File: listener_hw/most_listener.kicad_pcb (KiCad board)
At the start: 2 copper layers, 125 x 80 mm, 153 parts, among them J1 1-1394640-1, J2 ANALYSER, J3 I2S, J4 VBAT_IN, J5 PLR135/T10, J6 PLT133/T10W, J7 RCA 75R, J8 LINE L, J9 LINE R, M1 Tang Nano 20K, M2 ESP32-DevKitC-VIE, U1 74LVC1G34, U10 TPS2553DBVR, U11 74LVC1G123, U12 DIR9001, U13 SRC4192, U14 LP5907MFX-3.3, U15 PCM5102A, U16 LP5907MFX-3.3, U2 74LVC1G157, U3 74LVC1G125, U4 74LVC1G123, U5 TPS7B8133DRV, U6 LMR38020F, U7 Si514, U8 LP5907MFX-3.3, U9 74LVC1G79, X1 24.576MHz

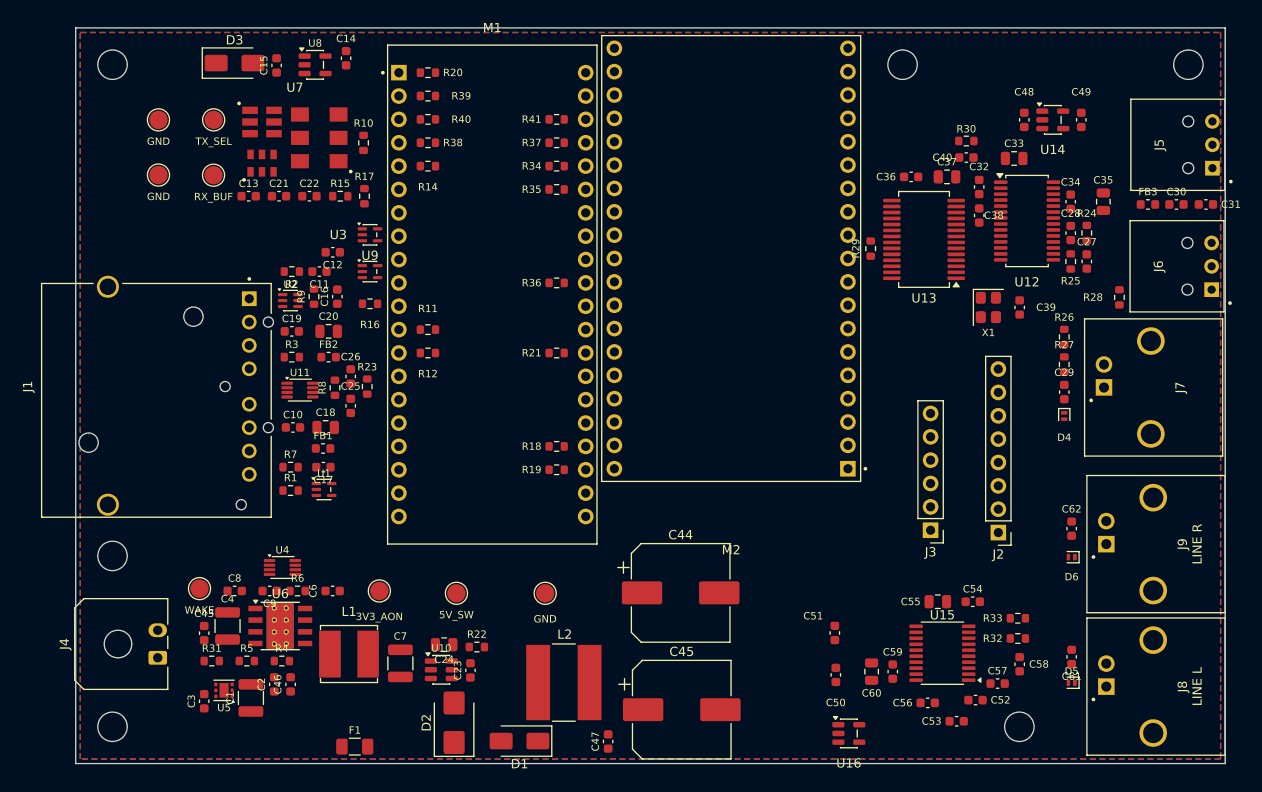
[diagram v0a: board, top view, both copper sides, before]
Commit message: Board: silk pass on the final placement - DRC with no error and no warning
The user settled the placement (moving C44, H4 and M2 a little last) and
asked for the silkscreen to be put right: 94 silk warnings before, none now.

- The edge connectors' own silk no longer reaches the board edge: the MOST
  header (J1), the TOSLINK modules (J5, J6) and the RCA jacks (J7, J8, J9)
  have their outline open on the port side, the sides ending 0.4 mm behind
  the port face (for J1, 0.4 mm inside the edge its foot line marks); the
  board's copies were refreshed from the library, so they match it. J4, a
  KiCad library part, moved 0.6 mm in from the left edge instead.
- Every silk text was placed again: the first spot around its part that
  touches no pad, no silk line and no other text and stays 0.4 mm inside the
  edge - 0.8 mm text for passives, 1.0 mm for ICs, modules and connectors,
  nothing smaller; M1, M2 and J1 carry their names inside their outlines,
  J8/J9 their LINE L/R, the test points their net names. The last three
  (C10, C18, R5) were set by hand.
- H4 back to 4.0 mm from the bottom edge; the antenna keep-out follows M2.

DRC with --schematic-parity: no error, no warning, no difference from the
sheet; 367 unconnected items - the routing is next.

Co-Authored-By: Claude Opus 5.5 <noreply@anthropic.com>
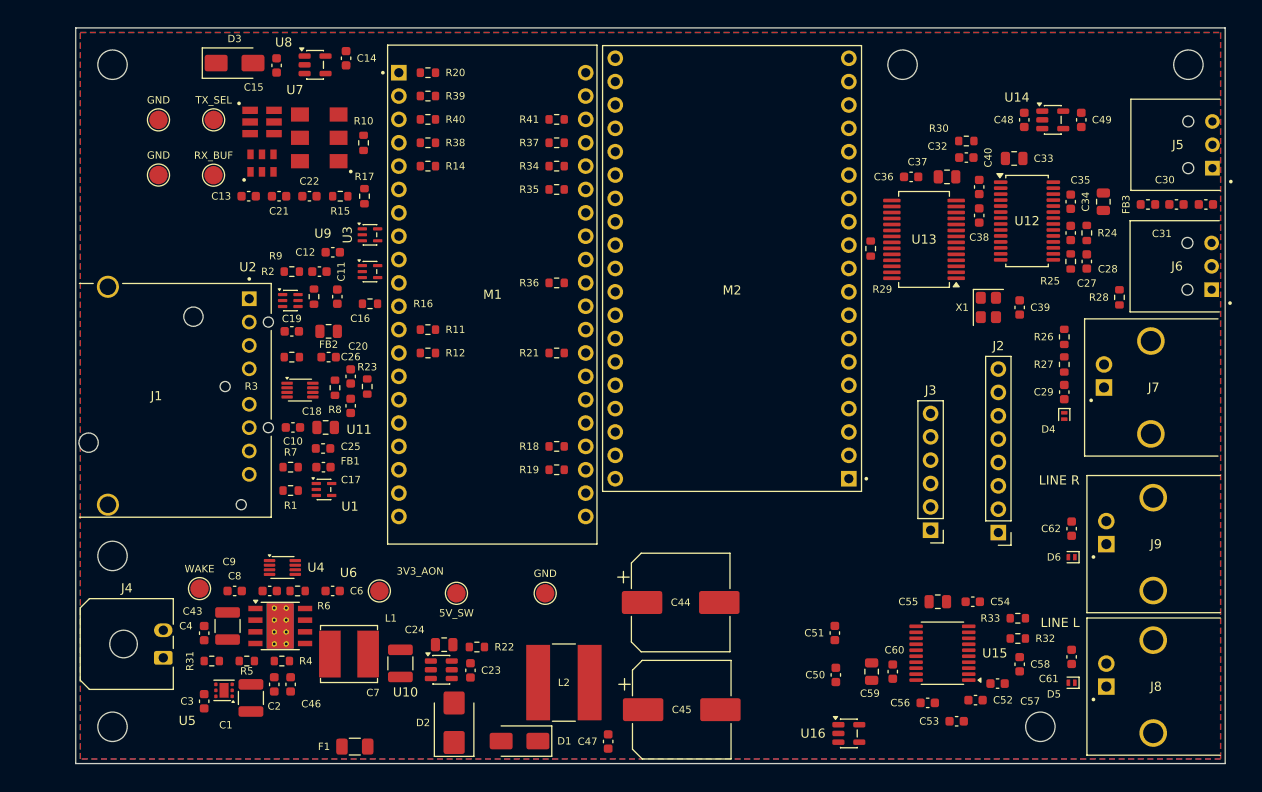
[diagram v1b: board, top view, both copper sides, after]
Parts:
- moved H4 2.29 mm to (104.9, 76.0)
- moved M2 1.09 mm to (71.4, 26.2)
- moved C44 1.04 mm to (65.8, 62.5)
- moved J4 0.60 mm to (9.52, 68.5)

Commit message: Board: routed - one ground plane below, crossed only by short jumpers; signals and supplies on top
- supplies laid by hand: the 5 V trunk 1 mm wide from C7 up the left edge under J1 and along
  the top edge; VBAT from the input caps round the bottom into C43, C4 and U6; 3V3_AON from the
  LDO with two jumpers (1.9 mm under VBAT at C3, 2.4 mm under the trunk into the front end);
  R4's sense on top under L1
- the host switch U10 with C23, C24 and R22 moved to M2's 5 V pin: /5V_HOST no longer crosses
  the signals from M1 to the right half
- a via beside every SMD ground pad; the top pour stitched to the plane about every 6 mm
- signals on top, the crossings as jumpers: 75, 174 mm in all, the longest 6.5 mm; 459 vias
- DRC: no error, no warning, nothing unconnected; the board matches the sheet

Co-Authored-By: Claude Opus 5.5 <noreply@anthropic.com>
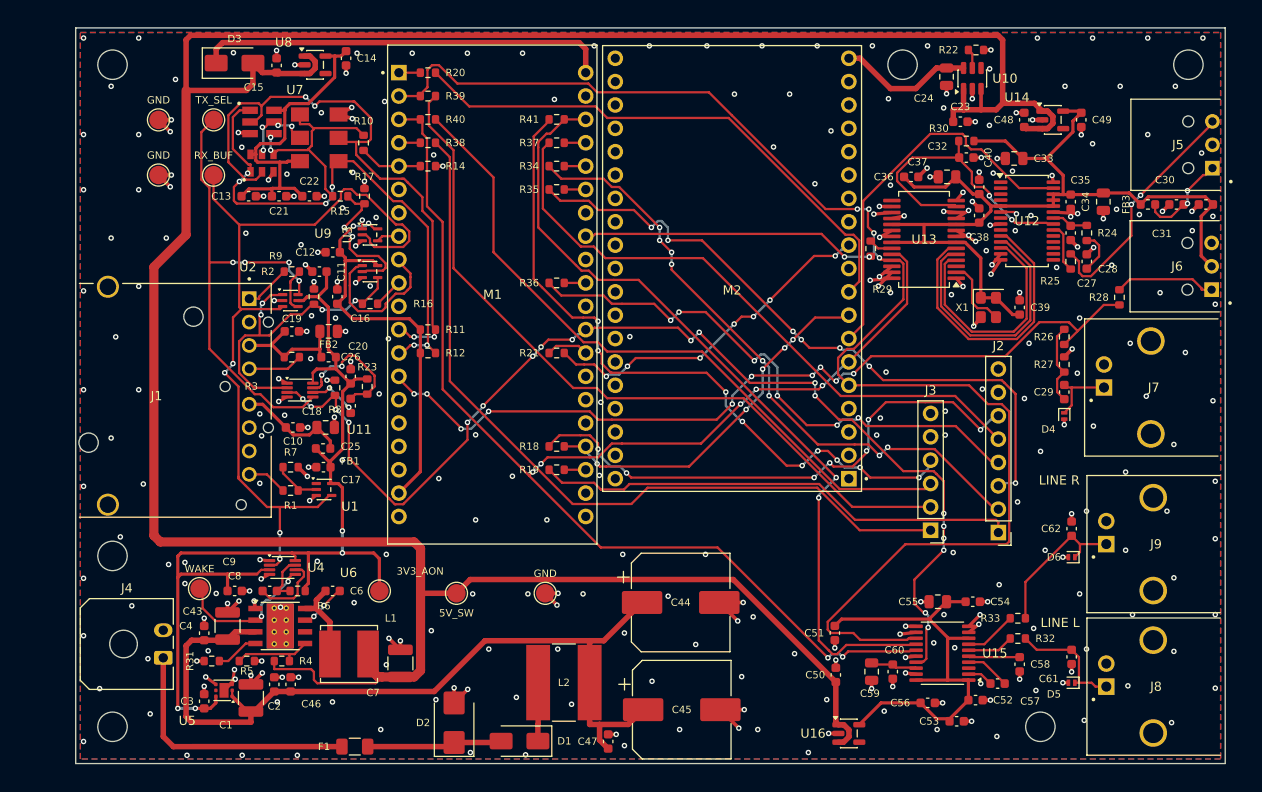
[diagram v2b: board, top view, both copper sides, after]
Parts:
- moved U10 86.4 mm to (97.5, 5.50), turned to 90 degrees
- moved R22 84.6 mm to (97.9, 2.40)
- moved C24 82.5 mm to (94.7, 5.31), turned to -90 degrees
- moved C23 80.0 mm to (96.2, 10.2), turned to 0 degrees
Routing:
- net 5V_SW: track 0.00 -> 316.1 mm
- net GND: track 0.00 -> 152.5 mm, vias 0 -> 316
- net /I2S_BCLK_F: track 0.00 -> 151.6 mm, vias 0 -> 4
- net /I2S_LRCK_F: track 0.00 -> 150.1 mm, vias 0 -> 7
- net /LOCK: track 0.00 -> 116.9 mm, vias 0 -> 19
- net 3V3_AON: track 0.00 -> 109.5 mm, vias 0 -> 4
- net 3V3_DA: track 0.00 -> 101.6 mm
- net VBAT_P: track 0.00 -> 93.8 mm
- net /SPDIF_F: track 0.00 -> 91.0 mm, vias 0 -> 10
- net /I2S_DOUT_F: track 0.00 -> 88.1 mm, vias 0 -> 2
- net /RX_BUF: track 0.00 -> 87.7 mm, vias 0 -> 4
- net Net-(J3-MCLK): track 0.00 -> 87.0 mm
- net Net-(J3-BCLK): track 0.00 -> 82.8 mm
- net Net-(J3-LRCK): track 0.00 -> 75.5 mm
- net Net-(J3-DOUT): track 0.00 -> 74.5 mm, vias 0 -> 9
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
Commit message: Board v1.2: pins swapped on the FPGA and host modules - the bus under M2 runs without a crossing, 33 jumpers instead of 75
- M1: every line bound for the right half leaves the right row in the order it meets J2, J3,
  the DAC and the host; LOCK and S/PDIF swap their LCD-only pins (LOCK on the left row beside
  U11); U13 gets its own copies of BCLK and LRCK (pins 73, 74) and returns DIN2 on 75, over the
  top of the module; PA_EN held low, as the module's amplifier now shares pins 54..56 with J2
- M2: BCLK IO22, LRCK IO23, DIN IO21, UART RX IO4 / TX IO15, OPT_ERR IO13 - on the row that
  faces M1; firmware and its pin table follow
- J2 now 1 SD0, 2 SD1, 3 FS, 4 MCLK, 5 UART_TX, 6 BCLK; J3 now 1 MCLK, 2 DOUT, 3 LRCK, 4 BCLK;
  the silk names every contact; "v1.2" in the silk, rev 1.2 on sheet and board
- the user's fixes: 5V_SW down left of C50 into U16, C50/C51 moved to U16; 3V3_SW into R12
  from below, so SCL/SDA pass between R11 and R12; U7's unused CLK- numbered on one land
  pattern only, so its three pads need no copper
- C23 at U10's input 10u: the host's radio pulses come out of it, not over the 17 cm trunk
- the 33R series resistors under M1 follow their pins; R20/R21 drawn at M2
- checks: DRC no error, no warning, nothing unconnected, matches the sheet; the pin maps of the
  .cst, the top module, the firmware and the sheet agree; Gowin timing PASS (clk_1024
  77.6 MHz, clk_s 119.3 MHz); check_all 24/24, and it now also fails on unconnected items

Co-Authored-By: Claude Opus 5.5 <noreply@anthropic.com>
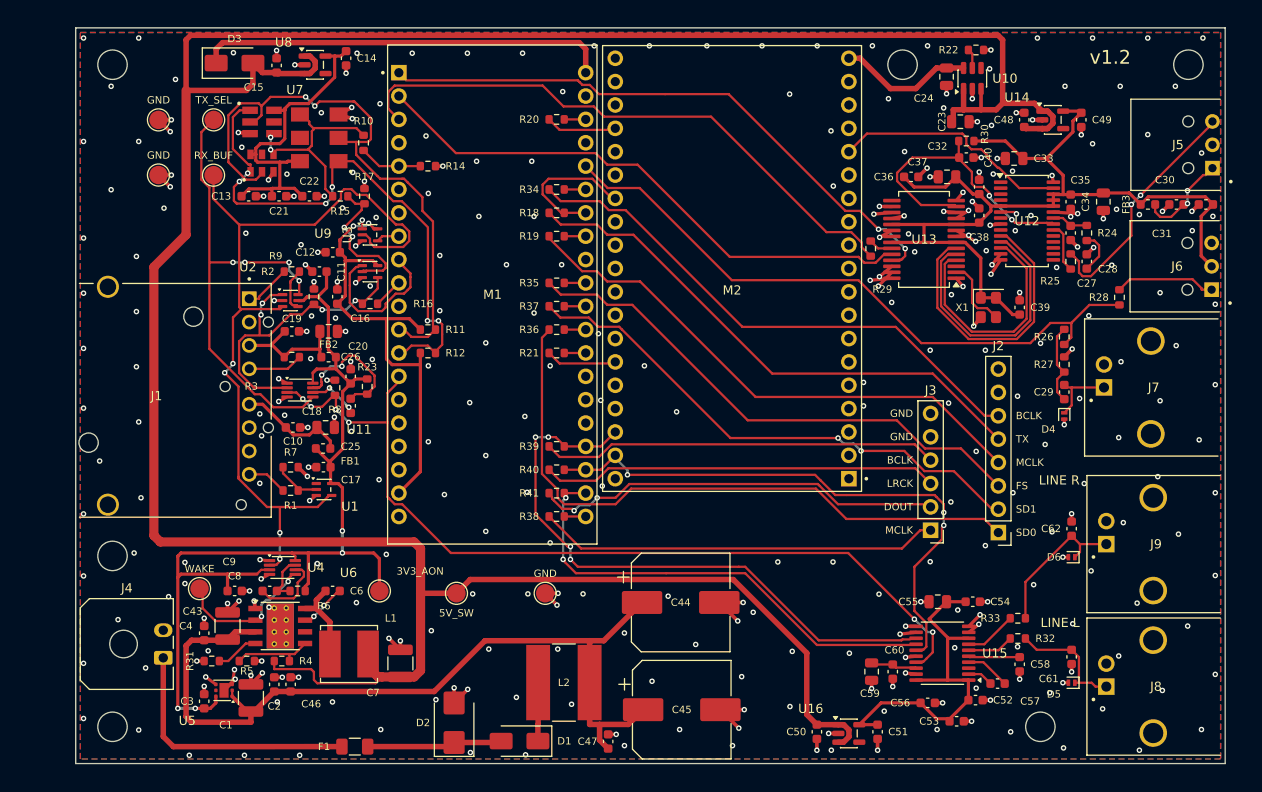
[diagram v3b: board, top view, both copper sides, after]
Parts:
- C23: value 100n -> 10u 16V; footprint Capacitor_SMD:C_0603_1608Metric -> Capacitor_SMD:C_0805_2012Metric
- moved R38 43.0 mm to (52.3, 53.1), turned to 180 degrees
- moved R41 40.6 mm to (52.3, 50.6)
- moved R39 40.6 mm to (52.3, 45.5), turned to 180 degrees
- moved R40 40.6 mm to (52.3, 48.0), turned to 180 degrees
- moved R18 25.4 mm to (52.3, 20.1)
- moved R19 25.4 mm to (52.3, 22.6)
- moved R37 17.8 mm to (52.3, 30.3)
- moved R20 14.9 mm to (52.3, 9.95), turned to 180 degrees
- moved C51 11.7 mm to (87.2, 76.5)
- moved R35 10.2 mm to (52.3, 27.7)
- moved C50 6.52 mm to (80.6, 76.5), turned to -90 degrees
- moved R36 5.08 mm to (52.3, 32.8)
- moved R34 2.54 mm to (52.3, 17.6)
- turned R21 to 180 degrees
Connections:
- J2 pad 1: Net-(J2-MCLK) -> Net-(J2-SD0)
- J2 pad 2: Net-(J2-BCLK) -> Net-(J2-SD1)
- J2 pad 4: Net-(J2-SD0) -> Net-(J2-MCLK)
- J2 pad 5: Net-(J2-SD1) -> Net-(J2-UART_TX)
- J2 pad 6: Net-(J2-UART_TX) -> Net-(J2-BCLK)
- J3 pad 2: Net-(J3-BCLK) -> Net-(J3-DOUT)
- J3 pad 4: Net-(J3-DOUT) -> Net-(J3-BCLK)
- M1 pad 1: /UART_RX_F -> /SRC_BCLK_F
- M1 pad 14: /SPDIF_F -> /LOCK
- M1 pad 2: /I2S_BCLK_F -> /SRC_LRCK_F
- M1 pad 23: /I2S_DOUT_F -> /UART_RX_F
- M1 pad 24: /SD1_F -> unconnected-(M1-80_SDIO_D2-Pad24)
- M1 pad 25: /BCLK_F -> /SPDIF_F
- M1 pad 26: /FS_F -> /BCLK_F
- M1 pad 27: unconnected-(M1-56_I2S_BCLK-Pad27) -> /UART_TX_F
- M1 pad 28: /I2S_DIN2_F -> /MCLK_F
- M1 pad 3: /I2S_LRCK_F -> /I2S_DIN2_F
- M1 pad 30: /SD0_F -> /FS_F
- M1 pad 31: unconnected-(M1-55_I2S_LRCK-Pad31) -> /SD1_F
- M1 pad 32: /LOCK -> /SD0_F
- M1 pad 37: /UART_TX_F -> /I2S_BCLK_F
- M1 pad 38: /MCLK_F -> /I2S_LRCK_F
- M1 pad 39: unconnected-(M1-53_EDID_CLK-Pad39) -> /I2S_DOUT_F
- M1 pad 4: /I2S_MCLK_F -> unconnected-(M1-85_SDIO_D1-Pad4)
- M1 pad 40: unconnected-(M1-52_EDID_DAT-Pad40) -> /I2S_MCLK_F
- M2 pad 11: Net-(M2-IO27) -> unconnected-(M2-IO27-Pad11)
- M2 pad 15: unconnected-(M2-IO13-Pad15) -> /OPT_ERR
- M2 pad 21: unconnected-(M2-IO23-Pad21) -> /I2S_LRCK_F
- M2 pad 22: unconnected-(M2-IO22-Pad22) -> /I2S_BCLK_F
- M2 pad 25: unconnected-(M2-IO21-Pad25) -> Net-(M2-IO21)
- M2 pad 32: unconnected-(M2-IO4-Pad32) -> /UART_TX_F
- M2 pad 35: unconnected-(M2-IO15-Pad35) -> Net-(M2-IO15)
- M2 pad 5: /I2S_BCLK_F -> unconnected-(M2-IO34-Pad5)
- M2 pad 6: /I2S_LRCK_F -> unconnected-(M2-IO35-Pad6)
- M2 pad 7: /OPT_ERR -> unconnected-(M2-IO32-Pad7)
- M2 pad 8: /UART_TX_F -> unconnected-(M2-IO33-Pad8)
- M2 pad 9: Net-(M2-IO25) -> unconnected-(M2-IO25-Pad9)
- R20 pad 2: Net-(M2-IO25) -> Net-(M2-IO15)
- R21 pad 2: Net-(M2-IO27) -> Net-(M2-IO21)
- U13 pad 24: /I2S_LRCK_F -> /SRC_LRCK_F
- U13 pad 25: /I2S_BCLK_F -> /SRC_BCLK_F
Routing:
- net /I2S_LRCK_F: track 150.1 -> 61.6 mm, vias 7 -> 3
- net /I2S_BCLK_F: track 151.6 -> 64.9 mm
- net /SRC_BCLK_F: track 0.00 -> 63.4 mm, vias 0 -> 2
- net /SRC_LRCK_F: track 0.00 -> 61.5 mm
- net Net-(M2-IO25): track 59.7 -> 0.00 mm
- net Net-(J3-MCLK): track 87.0 -> 43.8 mm
- net Net-(J3-BCLK): track 82.8 -> 43.2 mm
- net /I2S_DOUT_F: track 88.1 -> 50.9 mm
- net Net-(M2-IO27): track 36.5 -> 0.00 mm, vias 7 -> 0
- net /I2S_DIN2_F: track 31.1 -> 64.2 mm, vias 2 -> 0
- net Net-(J3-LRCK): track 75.5 -> 43.2 mm
- net Net-(J3-DOUT): track 74.5 -> 43.3 mm, vias 9 -> 2
- net /UART_TX_F: track 38.8 -> 15.6 mm, vias 5 -> 0
- net /LOCK: track 116.9 -> 94.4 mm, vias 19 -> 6
- net /SPDIF_F: track 91.0 -> 70.4 mm, vias 10 -> 0
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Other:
- board text added: "BCLK"
- board text added: "DOUT"
- board text added: "FS"
- board text added: "GND"
- board text added: "LRCK"
- board text added: "MCLK"
- board text added: "SD0"
- board text added: "SD1"
- board text added: "TX"
- board text added: "v1.2"
